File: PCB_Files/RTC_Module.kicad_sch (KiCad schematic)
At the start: 14 parts, among them J1 DZ254W-11-06-65, U1 DS3231SN#T&R, U2 AMS1117-3.3

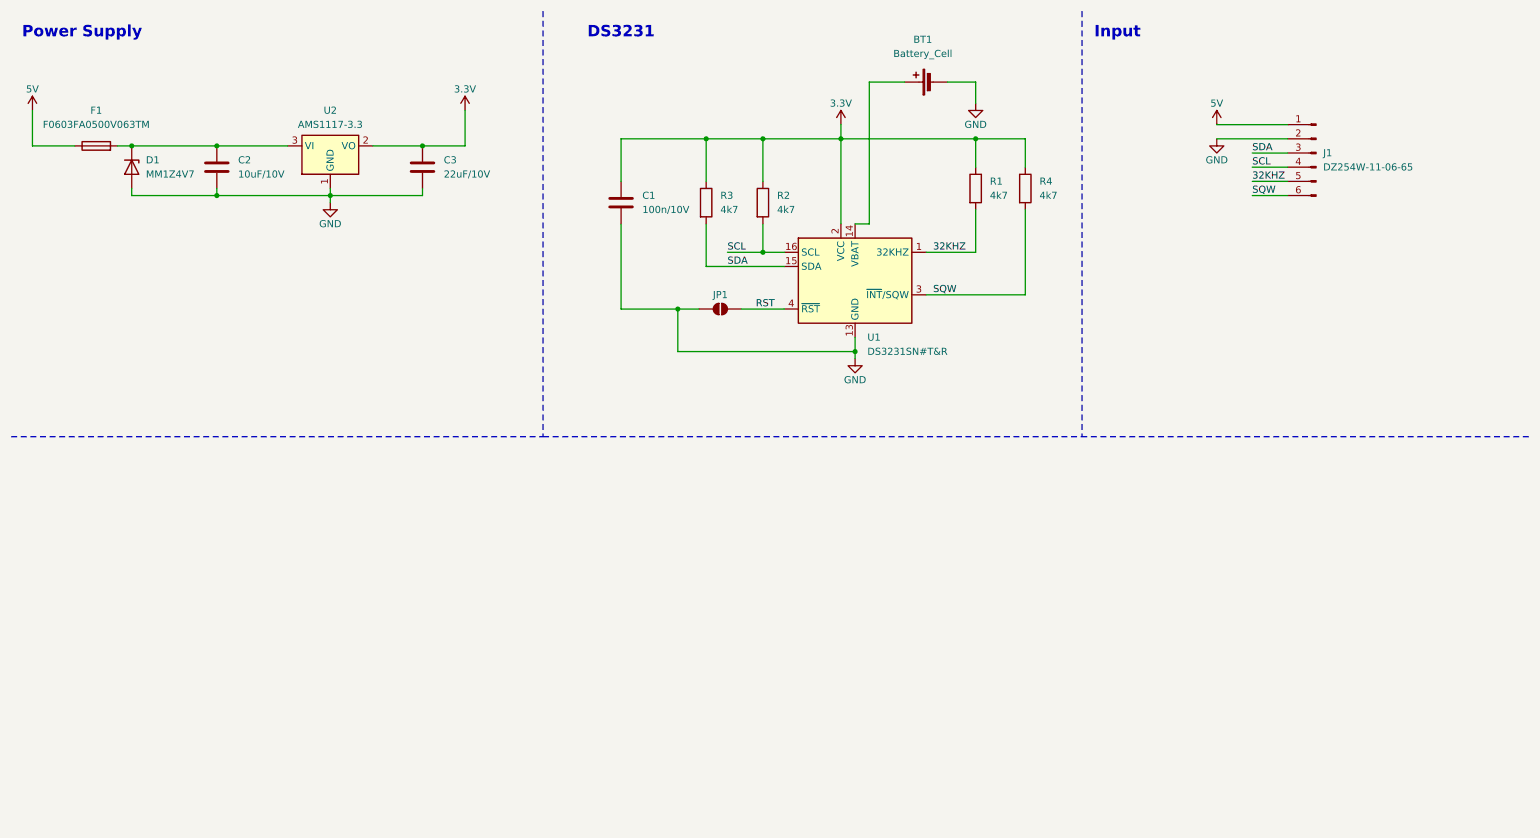
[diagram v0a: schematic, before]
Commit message: Added new RTC that is much cheaper.
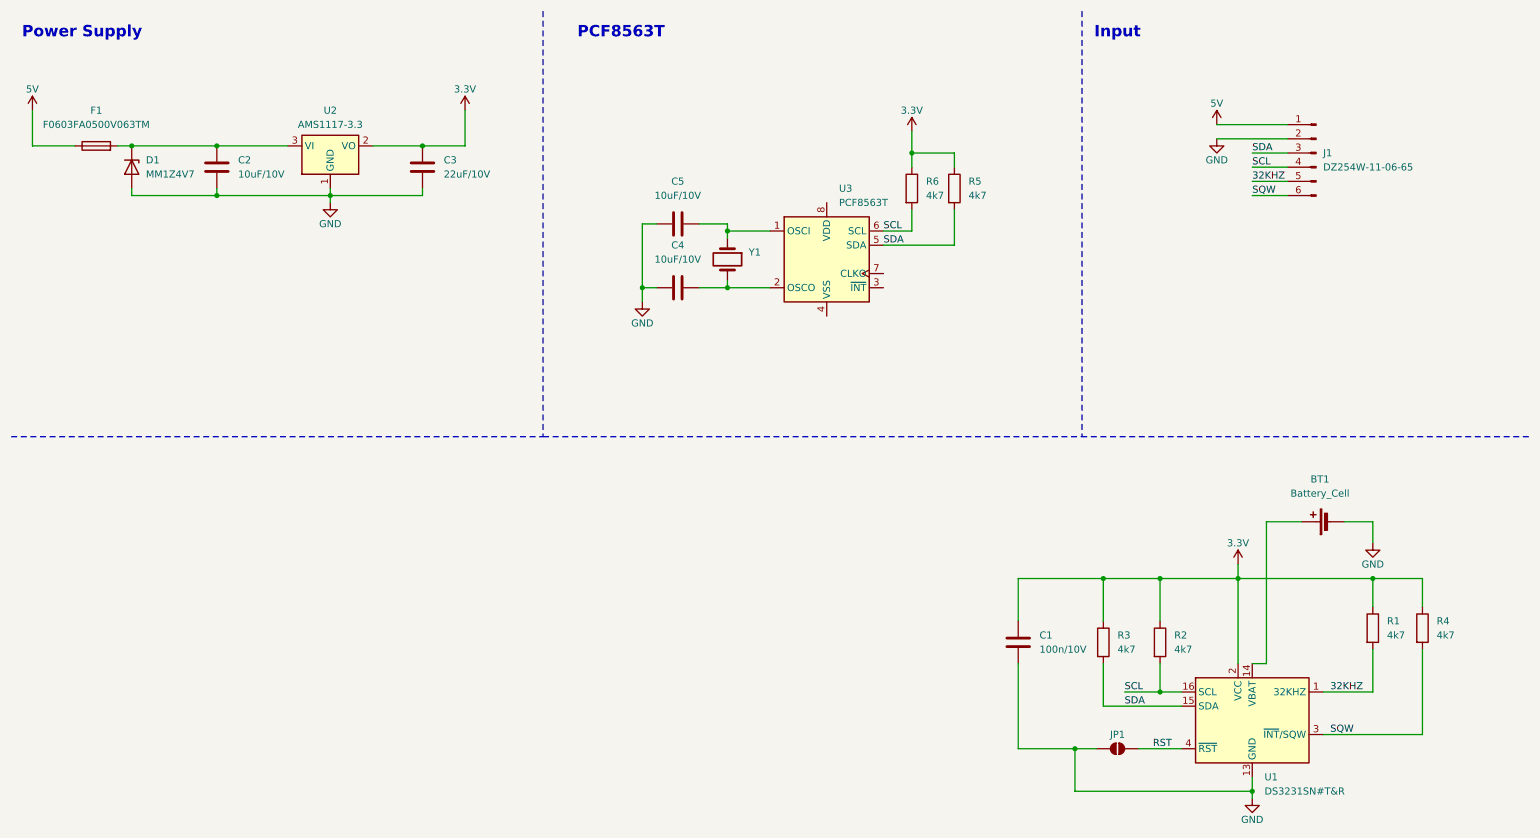
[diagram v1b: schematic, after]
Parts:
- added C4, C5: 10uF/10V, Capacitor_SMD:C_0805_2012Metric, symbol Device:C
- added R5, R6: 4k7, Resistor_SMD:R_0603_1608Metric, symbol Device:R
- added U3: PCF8563T, Package_SO:SOIC-8_3.9x4.9mm_P1.27mm, symbol Timer_RTC:PCF8563T
- added Y1: Q13FC13500004, Crystal:Crystal_SMD_MicroCrystal_CC7V-T1A-2Pin_3.2x1.5mm, symbol Device:Crystal
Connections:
- net 3.3V: now also R5.1, R6.1
- net GND: now also C4.2, C5.2
- net SCL: now also R6.2, U3.6 (SCL)
- net SDA: now also R5.2, U3.5 (SDA)
- new net: C5.1, U3.1 (OSCI), Y1.1
- new net: C4.1, U3.2 (OSCO), Y1.2
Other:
- note added: "PCF8563T"
- note removed: "DS3231"
- moved on the sheet: BT1, C1, JP1, R1, R2, R3, R4, U1
